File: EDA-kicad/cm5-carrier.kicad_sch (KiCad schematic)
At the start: 54 parts, among them J1 SJ2-35894B-SMT-TR, J3 USB4056-03-A, J5 FINGER, J6 SIM-G85D1160022HHR, SW1 VOL-, SW2 PROG, SW3 VOL+, SW4 POW, SW5 CHP-041B, SW6 PROG, SW7 VOL-, SW8 VOL+, SW9 POW, U1 Flash-LED-Lumiled, U10 Flash-LED-Lumiled, U2 CHARGER-SWITCHER-BQ25303JRTER, U3 BAT-MONITOR-BQ27530YZFT-G1, U4 BAT-STEP-UP-MIC2876-5.0YMT-TR, U5 BAT-CONNECTOR-FLTS22WR00, U6 GSM-GPS-EC25VFA-512-STD, U7 FPC15pin-1mm-pitch-F52Q-1A7H1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, U8 DAC-TLV320DAC3100IRHBR, U9 CODEC-TLV320AIC3204IRHBR

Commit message: fix USB C EDA files & add usb c pinout to schematic
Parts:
- removed B2: VIBR, SPIRIT-footprints:VIBRATION-PUI_HD-EMB1205-3-SC-R, symbol SPIRIT-components:VIBR
- removed C5, C6: USBC_capacitor_GRM033R60J334ME90D, SPIRIT-footprints:USBC_capacitor_CAPC0603X33N, symbol SPIRIT-components:USBC_capacitor_GRM033R60J334ME90D
- removed J3: USB4056-03-A, SPIRIT-footprints:USBC3-2, symbol SPIRIT-components:USB4056-03-A
- removed Module1: ComputeModule4-CM4, CM4IO:Raspberry-Pi-4-Compute-Module, symbol CM4IO:ComputeModule4-CM4
- removed R2, R3: CC-PULLDOWN-RESISTOR, SPIRIT-footprints:CC-PULLDOWN-RESISOTR, symbol SPIRIT-components:CC-PULLDOWN-RESISTOR
- removed SW1: VOL-, SPIRIT-footprints:buttonSW_TL3330_EWI, symbol SPIRIT-components:TL3330AF260QG
- removed SW2: PROG, SPIRIT-footprints:buttonSW_TL3330_EWI, symbol SPIRIT-components:TL3330AF260QG
- removed SW3: VOL+, SPIRIT-footprints:buttonSW_TL3330_EWI, symbol SPIRIT-components:TL3330AF260QG
- removed SW4: POW, SPIRIT-footprints:buttonSW_TL3330_EWI, symbol SPIRIT-components:TL3330AF260QG
- removed TP3, TP4, TP7, TP8: test-pad-1, SPIRIT-footprints:test-pad-1, symbol SPIRIT-components:test-pad-1
- removed U1: Flash-LED-Lumiled, SPIRIT-footprints:LUMILED-DIODFN449X305X210-3N, symbol SPIRIT-components:Flash-LED-Lumiled
- added J2: USBC-3-2-fix-USB4056-03-A_REVA2, SPIRIT-footprints:USBC-3-2-fix-GCT_USB4056-03-A_REVA2, symbol SPIRIT-components:USBC-3-2-fix-USB4056-03-A_REVA2
- added TP5, TP6: test-pad-1, SPIRIT-footprints:test-pad-1, symbol SPIRIT-components:test-pad-1
- renumbered J6 to J3, J5 to J4, Module2 to Module1, SW5 to SW1, SW6 to SW2, SW7 to SW3, SW8 to SW4, SW9 to SW5, TP9 to TP1, TP10 to TP2, TP1 to TP3, TP2 to TP4, TP5 to TP7, TP6 to TP8, TVS-PUSB3FR1 to TVS-PUSB1, U4 to U1, U5 to U2, U2 to U4, U10 to U5, U7 to U6, U9 to U7, U6 to U9
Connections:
- net CC1: now also J2.A5 (CC1)
- net CC2: now also J2.B5 (CC2)
- net D+: now also J2.A6 (DP1), J2.B6 (DP2)
- net D-: now also J2.A7 (DN1), J2.B7 (DN2)
- net GND: now also B1.P, J2.A1 (GND_A), J2.A12 (GND_A__1), J2.B1 (GND_B), J2.B12 (GND_B__1), J2.S1 (SHELL_GND), J2.S2 (SHELL_GND__1), J2.S3 (SHELL_GND__2), J2.S4 (SHELL_GND__3); no longer B1.N
- net RX1+: now also J2.A11 (SSRXP2), J2.B11 (SSRXP1)
- net RX1-: now also J2.A10 (SSRXN2), J2.B10 (SSRXN1)
- net TX1+: now also J2.A2 (SSTXP1), J2.B2 (SSTXP2)
- net TX1-: now also J2.A3 (SSTXN1), J2.B3 (SSTXN2)
- net USBC POW: now also J2.A4 (VBUS_A), J2.A9 (VBUS_A__1), J2.B4 (VBUS_B), J2.B9 (VBUS_B__1)
- net at Module1.48 (GPIO27), TP2.1 (A): now also B1.N
- new net: J2.B8 (SBU2), TP6.1 (A)
- new net: J2.A8 (SBU1), TP5.1 (A)
- no-connect marks 16 -> 10
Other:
- note added: "(Iphone 16 uses 2.0 XD)"
- note added: "CM5 CONNECTORS"
- note added: "Don't forget to check against the official RPi IO board!!!"
- note added: "LED and VIBRATOR CAN't be powered from GPIO!!!"
- note added: "USB C 3.2"
- note added: "USB C protection:"
- note added: "resistors are not needed in case of the CC pins because the cm5 already takes care of the negotiation/role assignment"
- note removed: "Capacitors in parallel:"
- note removed: "LED and VIBRATOR CAN't be power from GPIO!!!"
- note removed: "RX1"
- note removed: "RX2"
- note removed: "Resistors in series:"
- note removed: "TX1"
- note removed: "TX2"
- note removed: "USB C 3.0"
- moved on the sheet: C1, C2, C3, C4, DIS1, Module1A, Module1B, SW2, SW3, SW4, SW5, TP1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

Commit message: remove old text
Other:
- note removed: "todo add capacitors on tx and rx"
- note removed: "todo connect tx and rx pins to CM5"
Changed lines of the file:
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@@
 	(text "(Iphone 16 uses 2.0 XD)"
 		(exclude_from_sim no)
-		(at 528.828 99.568 0)
+		(at 525.272 106.426 0)
 		(effects
 			(font
@@
 		)
 	)
-	(text "todo connect tx and rx pins to CM5"
-		(exclude_from_sim no)
-		(at 516.382 104.14 0)
-		(effects
-			(font
-				(size 1.27 1.27)
-			)
-		)
-	)
-	(text "todo add capacitors on tx and rx\n"
-		(exclude_from_sim no)
-		(at 515.366 107.188 0)
-		(effects
-			(font
-				(size 1.27 1.27)
-			)
-		)
-	)
 	(text "check I2c connections od codec and display perhaps use mipi\n"
 		(exclude_from_sim no)
@@
 	(text "USB C 3.2"
 		(exclude_from_sim no)
-		(at 500.888 99.06 0)
+		(at 497.332 104.394 0)
 		(effects
 			(font
 				(size 4 4)
+				(thickness 0.8)
+				(bold yes)
 			)
 			(justify left bottom)
@@
 			"EOGHh7Bhh9WiHccRtmNYRgdXnqlU6jttb4QIEb5LRCZjhAgRIhykQLHuvd2BYc2dCBEiREBEJmOE"
 			"CBEiHLwQWjmwp1L3524W0RMjRDiYEZmMESJEiHCQYt+MwzAlMfI4RogQIVoyRogQIUKECBEiRNgP"
-			"Ii9jhAgRIhy8iALTESJEOED8Ly6skCOgCihyAAAAAElFTkSuQmCC"
+			"Ii9jhAgRIhy8iALTESJEOED8Ly6skCOgCihyAAAAAElFTkSuQmCCAAAAAAAAAAAAwH0BAAAAAAAw"
+			"AAAAAAAAAO9vrU9sVQAAAAAAAAAAAAAYpHhHl38AAND6PBlpVQAAAAAAgPshCUBhAQAAAAAAAFD8"
+			"PBlpVQAA8LfwIWlVAAAAAAAAAAAAAAAAAAAAAAAAAAAAAAAAAAAAAAAAAAAAAAAAAAAAAAAAAAAA"
+			"AAAAAAAAAAAAAAAAAAAAAAAAAAAAAAAAAAAAAAAAAAAAAAAAAAAAAAAAAAAAAAAAAAAAAAAAAAAA"
+			"AAAAAAAAAAAAAAAAAAAAAAAAAAAAAAAAAAAAAAAAAAAAAAAAAAAAAAAAAAAAAAAAAAAAAAAAAAAA"
+			"AAAAAAAAAAAAAAAAAAAAAAAAAAAAAAAAAAAAkQAAAAAAAABQ/DwZaVUAAMAcn0WXfwAAEPo8GWlV"
+			"AAAw/TwZaVUAAHkFAAAAAAAAAQAAAAAAAABA/DwZaVUAADD8PBlpVQAAeQUAAHkFAAAAAAAAAAAA"
+			"AAAAAAAAAAAAAAAAAAAAAAAAAAAAAAAAAPj7PBlpVQAA+Ps8GWlVAAAAAAAAAAAAAFB/AQAAAAAA"
+			"MAAAAAAAAAB/bq1PbFUAAAAAAAAAAAAAGKR4R5d/AABg/DwZaVUAAAAAAID7IQlAYQEAAAAAAADg"
+			"/TwZaVUAAPC38CFpVQAAAAAAAAAAAAAAAAAAAAAAAAAAAAAAAAAAAAAAAAAAAAAAAAAAAAAAAAAA"
+			"AAAAAAAAAAAAAAAAAAAAAAAAAAAAAAAAAAAAAAAAAAAAAAAAAAAAAAAAAAAAAAAAAAAAAAAAAAAA"
+			"AAAAAAAAAAAAAAAAAAAAAAAAAAAAAAAAAAAAAAAAAAAAAAAAAAAAAAAAAAAAAAAAAAAAAAAAAAAA"
+			"AAAAAAAAAAAAAAAAAAAAAAAAAAAAAAAAAAAAAJEAAAAAAAAA4P08GWlVAADAHJ9Fl38AAAAAAAAA"
+			"AAAAAAAAAAAAAAB6BQAAAAAAAAEAAAAAAAAA0P08GWlVAADA/TwZaVUAAHoFAAB6BQAAAAAAAAAA"
+			"AAAAAAAAAAAAAAAAAAAAAAAAAAAAAAAAAACI/TwZaVUAAIj9PBlpVQAAAAAAAAAAAADggAEAAAAA"
+			"ADAAAAAAAAAAj2ytT2xVAAAAAAAAAAAAABikeEeXfwAA8P08GWlVAAAAAACA+yEJQGEBAAAAAAAA"
+			"cP88GWlVAADwt/AhaVUAAAAAAAAAAAAAAAAAAAAAAAAAAAAAAAAAAAAAAAAAAAAAAAAAAAAAAAAA"
+			"AAAAAAAAAAAAAAAAAAAAAAAAAAAAAAAAAAAAAAAAAAAAAAAAAAAAAAAAAAAAAAAAAAAAAAAAAAAA"
+			"AAAAAAAAAAAAAAAAAAAAAAAAAAAAAAAAAAAAAAAAAAAAAAAAAA=="
 		)
 	)

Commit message: add cutout for battery
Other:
- note added: "Screen"
- note removed: "Sreen"
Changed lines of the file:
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@@
 			(font
 				(size 4 4)
+				(thickness 0.8)
+				(bold yes)
 			)
 			(justify left bottom)
@@
 		)
 	)
-	(text "Sreen\n"
+	(text "Screen\n"
 		(exclude_from_sim no)
 		(at 703.58 220.98 0)
@@
 			(font
 				(size 4 4)
+				(thickness 0.8)
+				(bold yes)
 			)
 			(justify left bottom)
@@
 			(font
 				(size 4 4)
+				(thickness 0.8)
+				(bold yes)
 			)
 			(justify left bottom)
@@
 			(font
 				(size 4 4)
+				(thickness 0.8)
+				(bold yes)
 			)
 			(justify left bottom)
@@
 			(font
 				(size 4 4)
+				(thickness 0.8)
+				(bold yes)
 			)
 			(justify left bottom)
@@
 			(font
 				(size 4 4)
+				(thickness 0.8)
+				(bold yes)
 			)
 			(justify left bottom)
@@
 			(font
 				(size 4 4)
-			)
-			(justify left bottom)
+				(thickness 0.8)
+				(bold yes)
+			)
+			(justify left bottom)

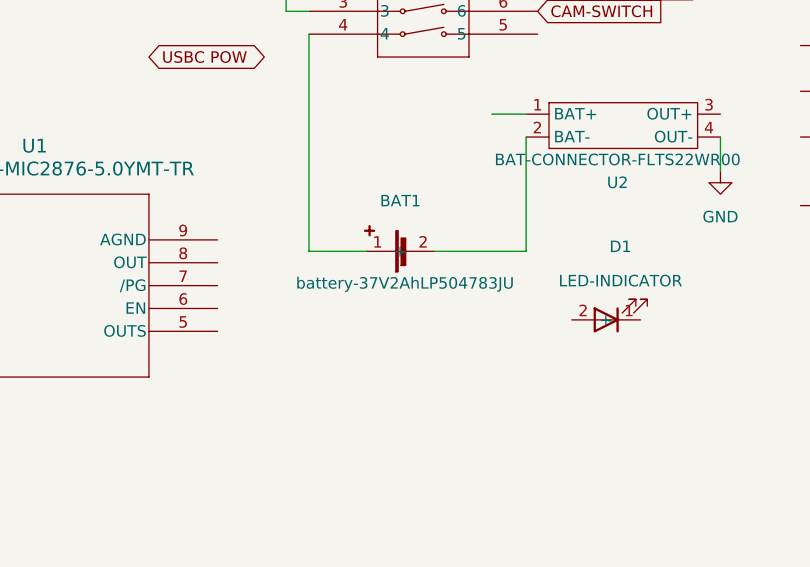
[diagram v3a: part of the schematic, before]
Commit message: New battery, its now a 3500mah one
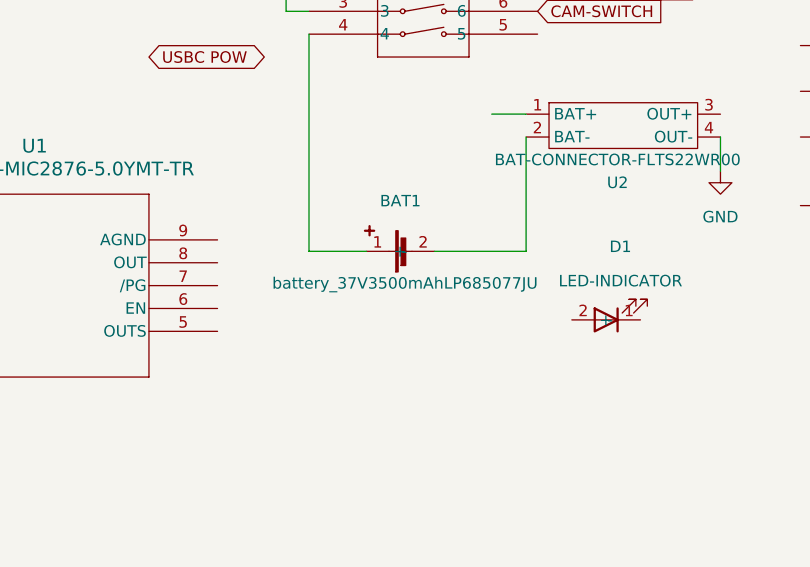
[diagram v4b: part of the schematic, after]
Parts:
- BAT1: value battery-37V2AhLP504783JU -> battery_37V3500mAhLP685077JU
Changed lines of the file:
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@@
 			)
 		)
-		(property "Value" "battery-37V2AhLP504783JU"
+		(property "Value" "battery_37V3500mAhLP685077JU"
 			(at 144.018 429.006 0)
 			(effects

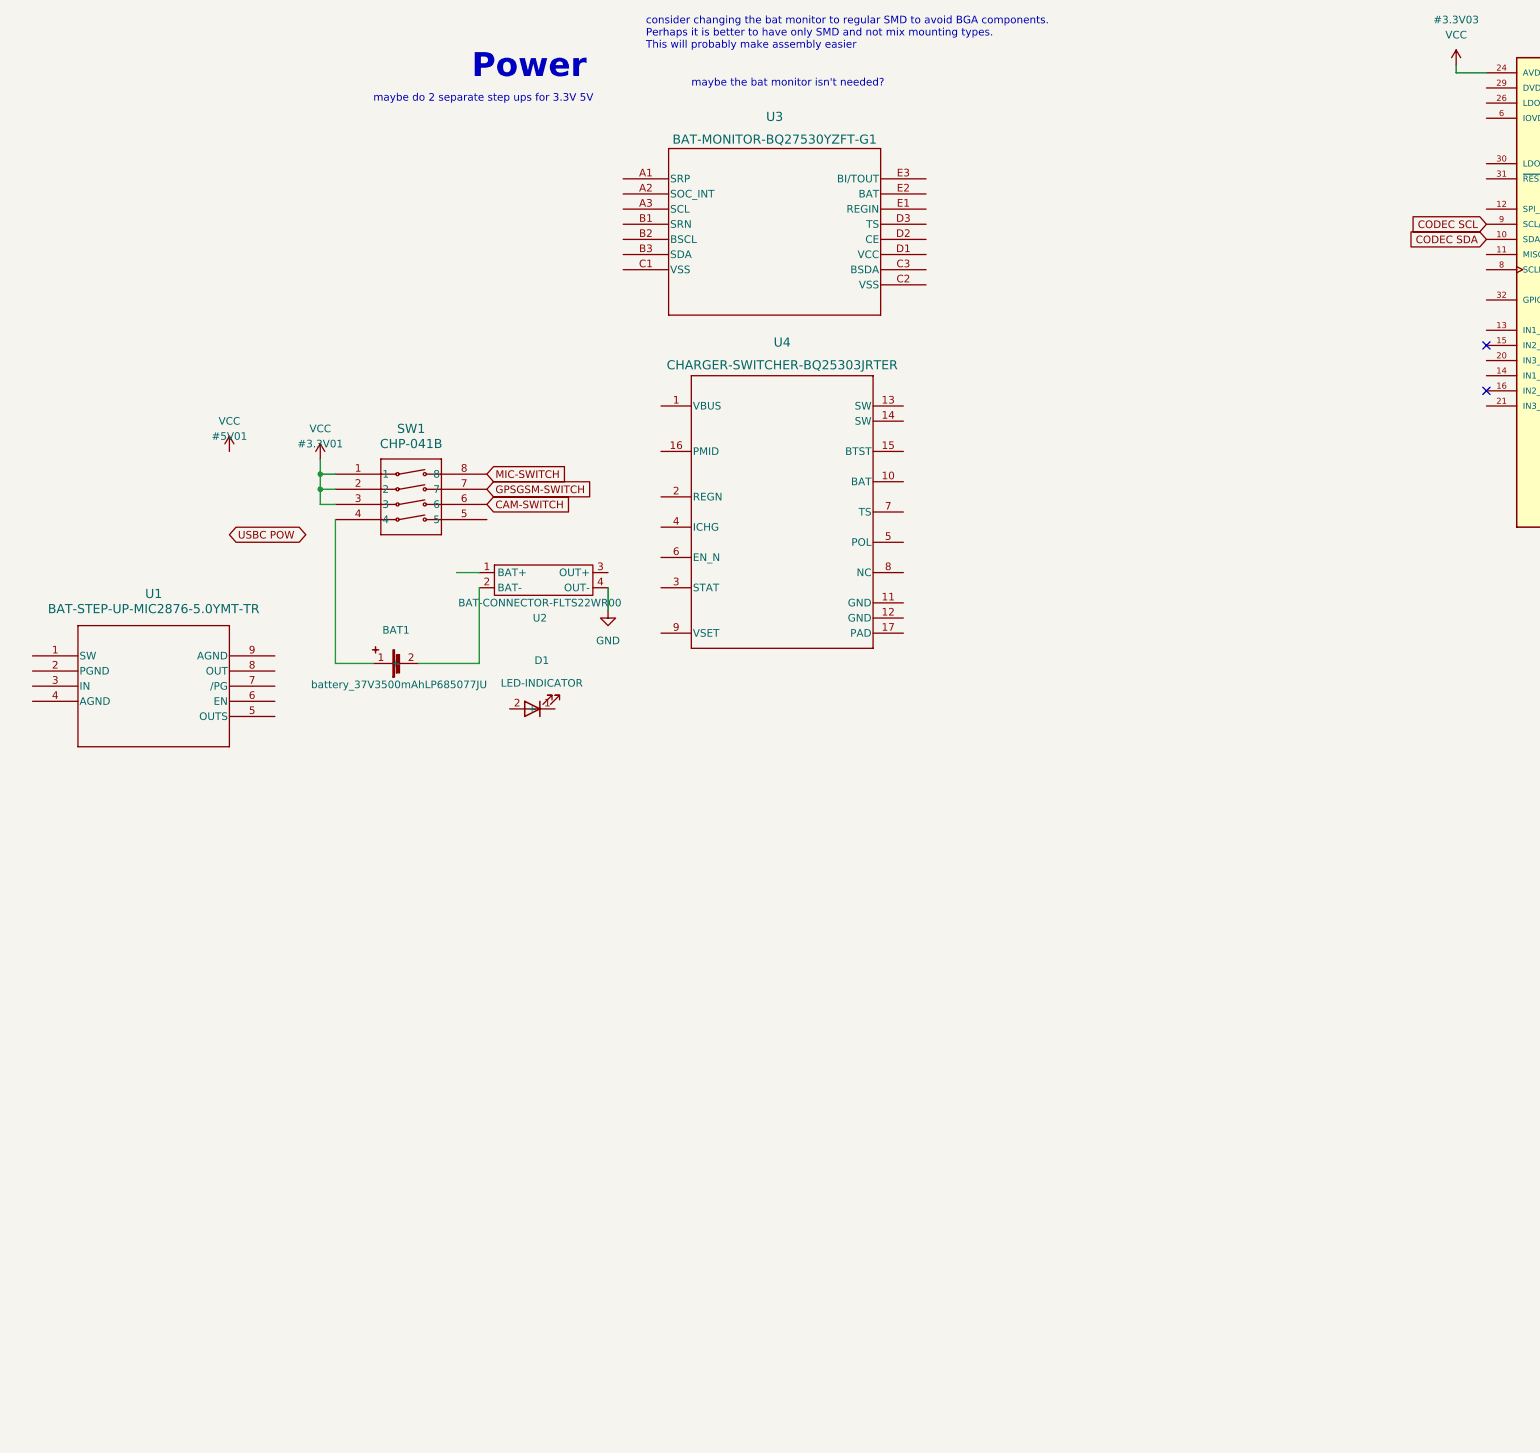
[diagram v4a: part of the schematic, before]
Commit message: Added the new power system. Some resistor values are still missing
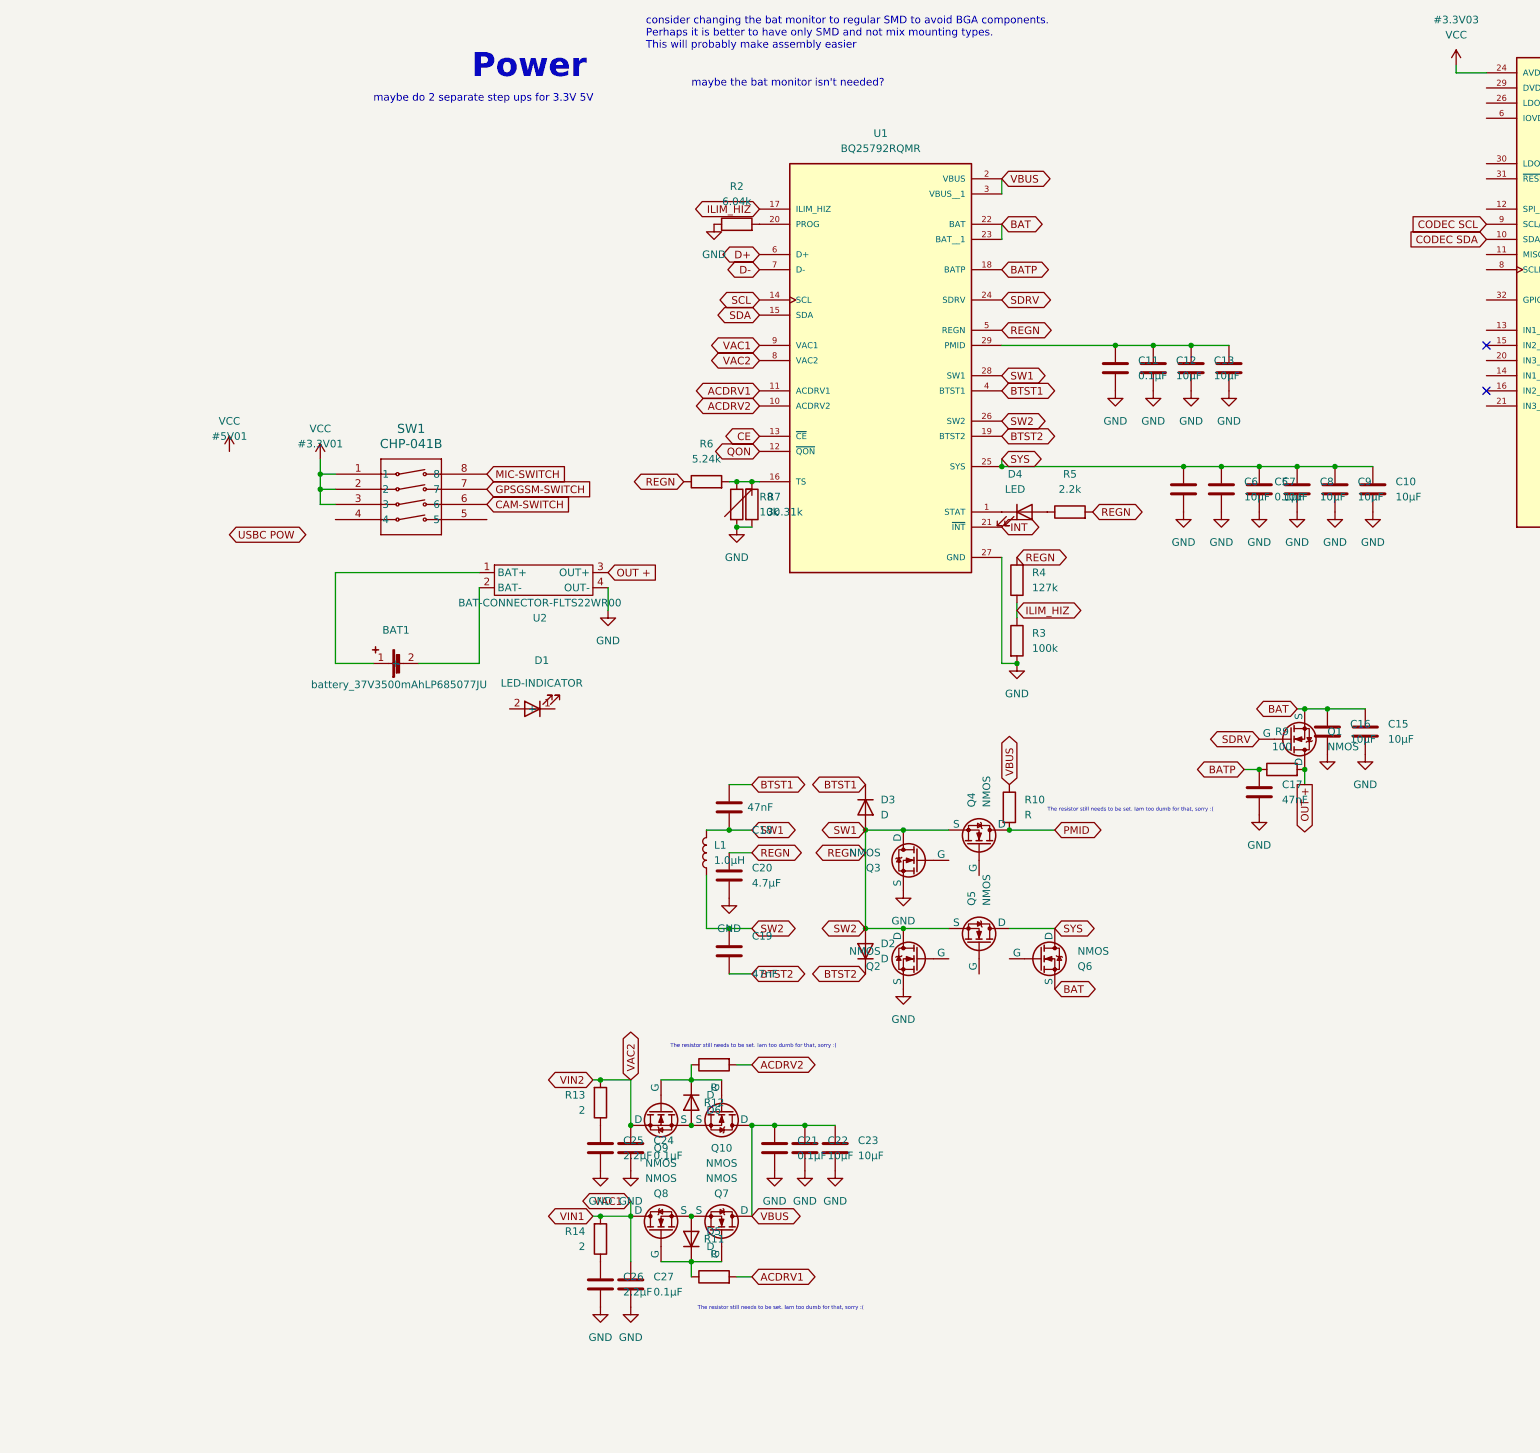
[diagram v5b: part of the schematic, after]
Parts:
- removed U1: BAT-STEP-UP-MIC2876-5.0YMT-TR, SPIRIT-footprints:BAT-STEP-UP-UDFN8_2X2_MCH, symbol SPIRIT-components:BAT-STEP-UP-MIC2876-5.0YMT-TR
- removed U3: BAT-MONITOR-BQ27530YZFT-G1, SPIRIT-footprints:BAT-MONITOR-YZF15_TEX, symbol SPIRIT-components:BAT-MONITOR-BQ27530YZFT-G1
- removed U4: CHARGER-SWITCHER-BQ25303JRTER, SPIRIT-footprints:CHARGER-SWITCHER-RTE0016C, symbol SPIRIT-components:CHARGER-SWITCHER-BQ25303JRTER
- added C10, C12, C13, C14, C15, C16, C22, C23, C6, C7, C8, C9: 10μF, symbol Device:C
- added C11, C21, C24, C27, C5: 0.1μF, symbol Device:C
- added C17, C18, C19: 47nF, symbol Device:C
- added C20: 4.7μF, symbol Device:C
- added C25, C26: 2.2μF, symbol Device:C
- added D2, D3, D5, D6: D, symbol Device:D
- added D4: LED, symbol Device:LED
- added L1: 1.0μH, symbol Device:L
- added Q1, Q10, Q2, Q3, Q4, Q5, Q6, Q7, Q8, Q9: NMOS, symbol Simulation_SPICE:NMOS
- added R10, R11, R12: R, symbol Device:R
- added R13, R14: 2, symbol Device:R
- added R2: 6.04k, symbol Device:R
- added R3: 100k, symbol Device:R
- added R4: 127k, symbol Device:R
- added R5: 2.2k, symbol Device:R
- added R6: 5.24k, symbol Device:R
- added R7: 30.31k, symbol Device:R
- added R8: 10k, symbol Device:R_Variable
- added R9: 100, symbol Device:R
- added U1: BQ25792RQMR, BQ25792RQMR:QFN40P400X400X100-29N, symbol BQ25792RQMR:BQ25792RQMR
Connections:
- net D+: now also U1.6 (D+)
- net D-: now also U1.7 (D-)
- net GND: now also C10.2, C11.2, C12.2, C13.2, C14.2, C15.2, C16.2, C17.2, C20.2, C21.2, C22.2, C23.2, C24.2, C25.2, C26.2, C27.2, C5.2, C6.2, C7.2, C8.2, C9.2, Q2.3 (S), Q3.3 (S), R2.1, R3.2, R7.2, R8.2, U1.27 (GND)
- net at BAT1.1 (+): now also U2.1 (BAT+); no longer SW1.4
- net OUT +: now reaches U2.3 (OUT+)
- net OUT +: now also Q1.1 (D), R9.2
- new net: C26.1, R14.1
- new net: D5.1 (K), Q7.2 (G), Q8.2 (G), R11.1
- new net: D5.2 (A), Q7.3 (S), Q8.3 (S)
- new net: C11.1, C12.1, C13.1, C14.1, U1.29 (PMID)
- new net: D6.1 (K), Q10.2 (G), Q9.2 (G), R12.1
- new net: D6.2 (A), Q10.3 (S), Q9.3 (S)
- new net: D4.1 (K), U1.1 (STAT)
- new net: D4.2 (A), R5.1
- new net: C25.1, R13.1
- new net: R6.2, R7.1, R8.1, U1.16 (TS)
- new net: R2.2, U1.20 (PROG)
- new net ACDRV1: R11.2, U1.11 (ACDRV1)
- new net ACDRV2: R12.2, U1.10 (ACDRV2)
- new net BAT: C15.1, C16.1, Q1.3 (S), Q6.3 (S), U1.22 (BAT), U1.23 (BAT__1)
- new net BATP: C17.1, R9.1, U1.18 (BATP)
- new net BTST1: C18.1, D3.1 (K), U1.4 (BTST1)
- new net BTST2: C19.2, D2.1 (K), U1.19 (BTST2)
- new net CE: U1.13 (~{CE})
- new net ILIM_HIZ: R3.1, R4.1, U1.17 (ILIM_HIZ)
- new net INT: U1.21 (~{INT})
- new net PMID: Q4.1 (D), R10.2
- new net QON: U1.12 (~{QON})
- new net REGN: C18.2, C19.1, C20.1, D2.2 (A), D3.2 (A), L1.1, L1.2, Q2.1 (D), Q3.1 (D), Q4.3 (S), Q5.3 (S), R4.2, R5.2, R6.1, U1.26 (SW2), U1.28 (SW1), U1.5 (REGN)
- new net SCL: U1.14 (SCL)
- new net SDA: U1.15 (SDA)
- new net SDRV: Q1.2 (G), U1.24 (SDRV)
- new net SYS: C10.1, C5.1, C6.1, C7.1, C8.1, C9.1, Q5.1 (D), Q6.1 (D), U1.25 (SYS)
- new net VAC1: C27.1, Q8.1 (D), R14.2, U1.9 (VAC1)
- new net VAC2: C24.1, Q9.1 (D), R13.2, U1.8 (VAC2)
- new net VBUS: C21.1, C22.1, C23.1, Q10.1 (D), Q7.1 (D), R10.1, U1.2 (VBUS), U1.3 (VBUS__1)
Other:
- note added: "The resistor still needs to be set. Iam too dumb for that, sorry :("
